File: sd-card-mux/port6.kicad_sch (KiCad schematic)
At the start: 10 parts, among them J201 47309-2285, U201 74LVC1G3157, U202 74LVC1G3157, U203 74LVC1G3157, U204 74LVC1G3157, U205 74LVC1G3157, U206 74LVC1G3157

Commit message: Added MCP23008 alternative
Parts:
- removed C201: 1u, Capacitor_SMD:C_0402_1005Metric, symbol Device:C_Small
- removed C202: 100n, Capacitor_SMD:C_0402_1005Metric, symbol Device:C_Small
- removed J201: 47309-2285, footprints:47309-2285, symbol 47309-2285:47309-2285
- removed JP201: PORTx, Connector_JST:JST_PH_S8B-PH-K_1x08_P2.00mm_Horizontal, symbol Connector_Generic:Conn_01x08
- removed U201, U202, U203, U204, U205, U206: 74LVC1G3157, Package_TO_SOT_SMD:SOT-363_SC-70-6, symbol 74LVC1G3157:74LVC1G3157
- added C801: 1u, Capacitor_SMD:C_0402_1005Metric, symbol Device:C_Small
- added C802: 100n, Capacitor_SMD:C_0402_1005Metric, symbol Device:C_Small
- added J801: 47309-2285, footprints:47309-2285, symbol 47309-2285:47309-2285
- added JP801: PORTx, Connector_JST:JST_PH_S8B-PH-K_1x08_P2.00mm_Horizontal, symbol Connector_Generic:Conn_01x08
- added U801, U802, U803, U804, U805, U806: 74LVC1G3157, Package_TO_SOT_SMD:SOT-363_SC-70-6, symbol 74LVC1G3157:74LVC1G3157
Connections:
- net +3V3: now also C801.1, C802.1, J801.P4 (VDD), JP801.4 (Pin_4), U801.5 (VCC), U802.5 (VCC), U803.5 (VCC), U804.5 (VCC), U805.5 (VCC), U806.5 (VCC)
- net CLKS: now also JP801.5 (Pin_5), U802.1
- net CMDS: now also JP801.3 (Pin_3), U801.1
- net DAT0S: now also JP801.7 (Pin_7), U803.1
- net DAT1S: now also JP801.8 (Pin_8), U804.1
- net DAT2S: now also JP801.1 (Pin_1), U805.1
- net DAT3S: now also JP801.2 (Pin_2), U806.1
- net GND: now also C801.2, C802.2, J801.G1 (GND_1), J801.G2 (GND_2), J801.P6 (VSS), JP801.6 (Pin_6), U801.2 (GND), U802.2 (GND), U803.2 (GND), U804.2 (GND), U805.2 (GND), U806.2 (GND)
- net SDIO_CLK: now also U802.3
- net SDIO_CMD: now also U801.3
- net SDIO_D0: now also U803.3
- net SDIO_D1: now also U804.3
- net SDIO_D2: now also U805.3
- net SDIO_D3: now also U806.3
- net SD_CLK: now also J801.P5 (CLK), U802.4
- net SD_CMD: now also J801.P3 (CMD), U801.4
- net SD_DAT0: now also J801.P7 (DAT0), U803.4
- net SD_DAT1: now also J801.P8 (DAT1), U804.4
- net SD_DAT2: now also J801.P1 (DAT2), U805.4
- net SD_DAT3: now also J801.P2 (CD/DAT3), U806.4
- new net PORT6: U801.6, U802.6, U803.6, U804.6, U805.6, U806.6
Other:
- note added: "TE Connectivity AMP-215079-8 + 215083-8"
- note removed: "TE Connectivity AMP series Female top entry 215079 Male to wire 215083"

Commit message: Addedd missing upload port
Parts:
- C801: LCSC Part# (none) -> C52923
- C802: LCSC Part# (none) -> C1525
- JP801: footprint Connector_JST:JST_PH_S8B-PH-K_1x08_P2.00mm_Horizontal -> footprints:ConnectorMicromatch-8
- U801, U802, U803, U804, U805, U806: LCSC Part# (none) -> C38663
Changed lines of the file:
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@@
+      (effects (font (size 1.27 1.27)) hide)
+    )
+    (property "LCSC Part#" "C52923" (id 4) (at 63.5 38.1 0)
       (effects (font (size 1.27 1.27)) hide)
     )
@@
       (effects (font (size 1.27 1.27)) hide)
     )
+    (property "LCSC Part#" "C1525" (id 4) (at 73.66 38.1 0)
+      (effects (font (size 1.27 1.27)) hide)
+    )
   )
   (symbol (lib_name "74LVC1G3157:74LVC1G3157_2") (lib_id "74LVC1G3157:74LVC1G3157") (at 175.26 43.18 0) (unit 1)
@@
     )
     (property "Datasheet" "https://www.ti.com/lit/ds/symlink/sn74lvc1g3157.pdf" (id 3) (at 175.26 43.18 0)
+      (effects (font (size 1.27 1.27)) hide)
+    )
+    (property "LCSC Part#" " C38663" (id 4) (at 175.26 43.18 0)
       (effects (font (size 1.27 1.27)) hide)
     )
@@
       (effects (font (size 1.27 1.27)) hide)
     )
+    (property "LCSC Part#" " C38663" (id 4) (at 175.26 66.04 0)
+      (effects (font (size 1.27 1.27)) hide)
+    )
   )
   (symbol (lib_id "74LVC1G3157:74LVC1G3157") (at 213.36 43.18 0) (unit 1)
@@
     )
     (property "Datasheet" "https://www.ti.com/lit/ds/symlink/sn74lvc1g3157.pdf" (id 3) (at 213.36 43.18 0)
+      (effects (font (size 1.27 1.27)) hide)
+    )
+    (property "LCSC Part#" " C38663" (id 4) (at 213.36 43.18 0)
       (effects (font (size 1.27 1.27)) hide)
     )
@@
       (effects (font (size 1.27 1.27)) hide)
     )
+    (property "LCSC Part#" " C38663" (id 4) (at 213.36 66.04 0)
+      (effects (font (size 1.27 1.27)) hide)
+    )
   )
   (symbol (lib_id "74LVC1G3157:74LVC1G3157") (at 213.36 88.9 0) (unit 1)
@@
     )
     (property "Datasheet" "https://www.ti.com/lit/ds/symlink/sn74lvc1g3157.pdf" (id 3) (at 213.36 88.9 0)
+      (effects (font (size 1.27 1.27)) hide)
+    )
+    (property "LCSC Part#" " C38663" (id 4) (at 213.36 88.9 0)
       (effects (font (size 1.27 1.27)) hide)
     )
@@
       (effects (font (size 1.27 1.27)) hide)
     )
+    (property "LCSC Part#" " C38663" (id 4) (at 213.36 111.76 0)
+      (effects (font (size 1.27 1.27)) hide)
+    )
   )
   (symbol (lib_id "Connector_Generic:Conn_01x08") (at 35.56 38.735 0) (mirror y) (unit 1)
@@
     (property "Reference" "JP801" (id 0) (at 37.592 25.635 0))
     (property "Value" "PORTx" (id 1) (at 37.592 27.9335 0))
-    (property "Footprint" "Connector_JST:JST_PH_S8B-PH-K_1x08_P2.00mm_Horizontal" (id 2) (at 35.56 38.735 0)
+    (property "Footprint" "footprints:ConnectorMicromatch-8" (id 2) (at 35.56 38.735 0)
       (effects (font (size 1.27 1.27)) hide)
     )

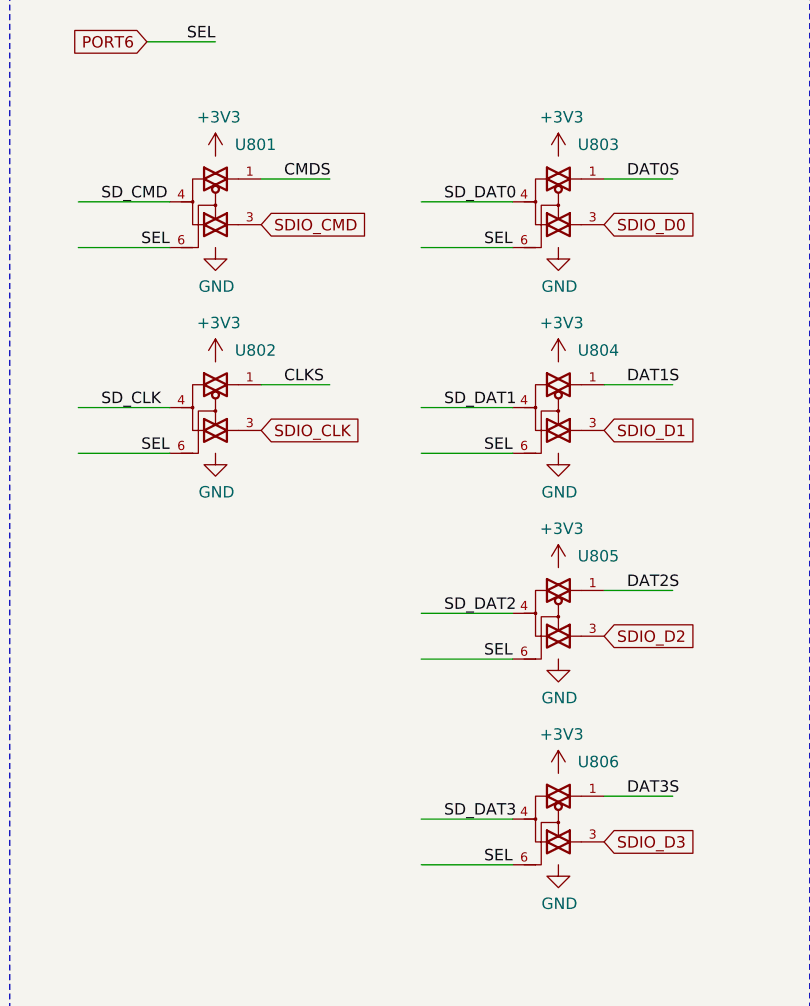
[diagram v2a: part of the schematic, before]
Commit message: Correction of inverted pins
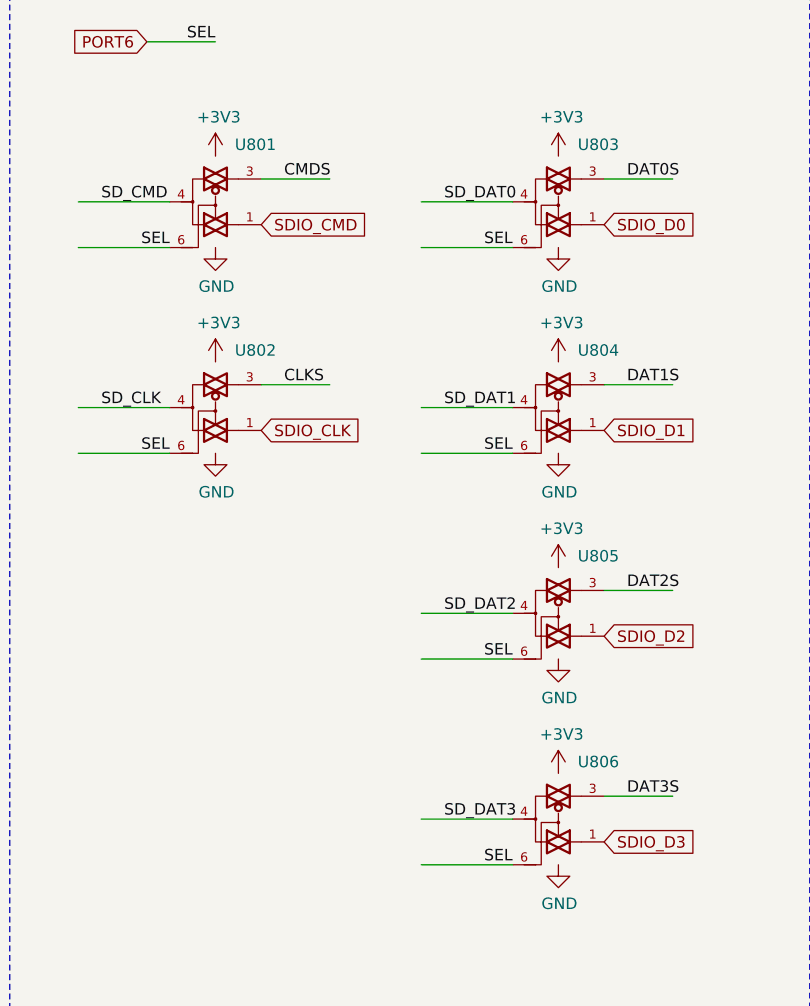
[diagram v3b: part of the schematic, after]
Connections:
- net CLKS: now also U802.3; no longer U802.1
- net CMDS: now also U801.3; no longer U801.1
- net DAT0S: now also U803.3; no longer U803.1
- net DAT1S: now also U804.3; no longer U804.1
- net DAT2S: now also U805.3; no longer U805.1
- net DAT3S: now also U806.3; no longer U806.1
- net SDIO_CLK: now also U802.1; no longer U802.3
- net SDIO_CMD: now also U801.1; no longer U801.3
- net SDIO_D0: now also U803.1; no longer U803.3
- net SDIO_D1: now also U804.1; no longer U804.3
- net SDIO_D2: now also U805.1; no longer U805.3
- net SDIO_D3: now also U806.1; no longer U806.3
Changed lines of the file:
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@@
 (kicad_sch (version 20200608) (host eeschema "(5.99.0-1973-g8c57821e9)")
-  (page 1 9)
+  (page 8 9)
   (paper "A4")
   (junction (at 63.5 33.02))
@@
     )
   )
-  (symbol (lib_id "74LVC1G3157:74LVC1G3157") (at 175.26 66.04 0) (unit 1)
+  (symbol (lib_name "74LVC1G3157:74LVC1G3157_1") (lib_id "74LVC1G3157:74LVC1G3157") (at 175.26 66.04 0) (unit 1)
     (in_bom yes) (on_board yes)
     (property "Reference" "U802" (id 0) (at 179.705 59.69 0))
@@
     )
   )
-  (symbol (lib_id "74LVC1G3157:74LVC1G3157") (at 213.36 43.18 0) (unit 1)
+  (symbol (lib_name "74LVC1G3157:74LVC1G3157_3") (lib_id "74LVC1G3157:74LVC1G3157") (at 213.36 43.18 0) (unit 1)
     (in_bom yes) (on_board yes)
     (property "Reference" "U803" (id 0) (at 217.805 36.83 0))
@@
     )
   )
-  (symbol (lib_id "74LVC1G3157:74LVC1G3157") (at 213.36 66.04 0) (unit 1)
+  (symbol (lib_name "74LVC1G3157:74LVC1G3157_4") (lib_id "74LVC1G3157:74LVC1G3157") (at 213.36 66.04 0) (unit 1)
     (in_bom yes) (on_board yes)
     (property "Reference" "U804" (id 0) (at 217.805 59.69 0))
@@
     )
   )
-  (symbol (lib_id "74LVC1G3157:74LVC1G3157") (at 213.36 88.9 0) (unit 1)
+  (symbol (lib_name "74LVC1G3157:74LVC1G3157_5") (lib_id "74LVC1G3157:74LVC1G3157") (at 213.36 88.9 0) (unit 1)
     (in_bom yes) (on_board yes)
     (property "Reference" "U805" (id 0) (at 217.805 82.55 0))

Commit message: Removal of host port and preparation for manufacturing
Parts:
- J801: Mechanical (none) -> T
- JP801: Mechanical (none) -> T; TME Part# (none) -> MM2x5
- U801, U802, U803, U804, U805, U806: LCSC Part# C38663 -> C265126; Rotation (none) -> 0
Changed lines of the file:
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@@
       (effects (font (size 1.27 1.27)) hide)
     )
-    (property "LCSC Part#" " C38663" (id 4) (at 175.26 43.18 0)
+    (property "LCSC Part#" "C265126" (id 4) (at 175.26 43.18 0)
+      (effects (font (size 1.27 1.27)) hide)
+    )
+    (property "Rotation" "0" (id 4) (at 175.26 43.18 0)
       (effects (font (size 1.27 1.27)) hide)
     )
@@
       (effects (font (size 1.27 1.27)) hide)
     )
-    (property "LCSC Part#" " C38663" (id 4) (at 175.26 66.04 0)
+    (property "LCSC Part#" "C265126" (id 4) (at 175.26 66.04 0)
+      (effects (font (size 1.27 1.27)) hide)
+    )
+    (property "Rotation" "0" (id 4) (at 175.26 66.04 0)
       (effects (font (size 1.27 1.27)) hide)
     )
@@
       (effects (font (size 1.27 1.27)) hide)
     )
-    (property "LCSC Part#" " C38663" (id 4) (at 213.36 43.18 0)
+    (property "LCSC Part#" "C265126" (id 4) (at 213.36 43.18 0)
+      (effects (font (size 1.27 1.27)) hide)
+    )
+    (property "Rotation" "0" (id 4) (at 213.36 43.18 0)
       (effects (font (size 1.27 1.27)) hide)
     )
@@
       (effects (font (size 1.27 1.27)) hide)
     )
-    (property "LCSC Part#" " C38663" (id 4) (at 213.36 66.04 0)
+    (property "LCSC Part#" "C265126" (id 4) (at 213.36 66.04 0)
+      (effects (font (size 1.27 1.27)) hide)
+    )
+    (property "Rotation" "0" (id 4) (at 213.36 66.04 0)
       (effects (font (size 1.27 1.27)) hide)
     )
@@
       (effects (font (size 1.27 1.27)) hide)
     )
-    (property "LCSC Part#" " C38663" (id 4) (at 213.36 88.9 0)
+    (property "LCSC Part#" "C265126" (id 4) (at 213.36 88.9 0)
+      (effects (font (size 1.27 1.27)) hide)
+    )
+    (property "Rotation" "0" (id 4) (at 213.36 88.9 0)
       (effects (font (size 1.27 1.27)) hide)
     )
@@
       (effects (font (size 1.27 1.27)) hide)
     )
-    (property "LCSC Part#" " C38663" (id 4) (at 213.36 111.76 0)
+    (property "LCSC Part#" "C265126" (id 4) (at 213.36 111.76 0)
+      (effects (font (size 1.27 1.27)) hide)
+    )
+    (property "Rotation" "0" (id 4) (at 213.36 111.76 0)
       (effects (font (size 1.27 1.27)) hide)
     )
@@
     )
     (property "Datasheet" "~" (id 3) (at 35.56 38.735 0)
+      (effects (font (size 1.27 1.27)) hide)
+    )
+    (property "TME Part#" "MM2x5" (id 4) (at 35.56 38.735 0)
+      (effects (font (size 1.27 1.27)) hide)
+    )
+    (property "Mechanical" "T" (id 4) (at 35.56 38.735 0)
       (effects (font (size 1.27 1.27)) hide)
     )
@@
       (effects (font (size 1.27 1.27)) (justify left) hide)
     )
+    (property "Mechanical" "T" (id 4) (at 66.04 88.265 0)
+      (effects (font (size 1.27 1.27)) hide)
+    )
   )
